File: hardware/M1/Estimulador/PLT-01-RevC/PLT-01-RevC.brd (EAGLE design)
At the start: 92.7 x 64.8 mm, 57 parts, among them T1 2N2222, T2 2N2222, T3 2N2222, T4 2N2222, T5 2N2222, T6 2N2222

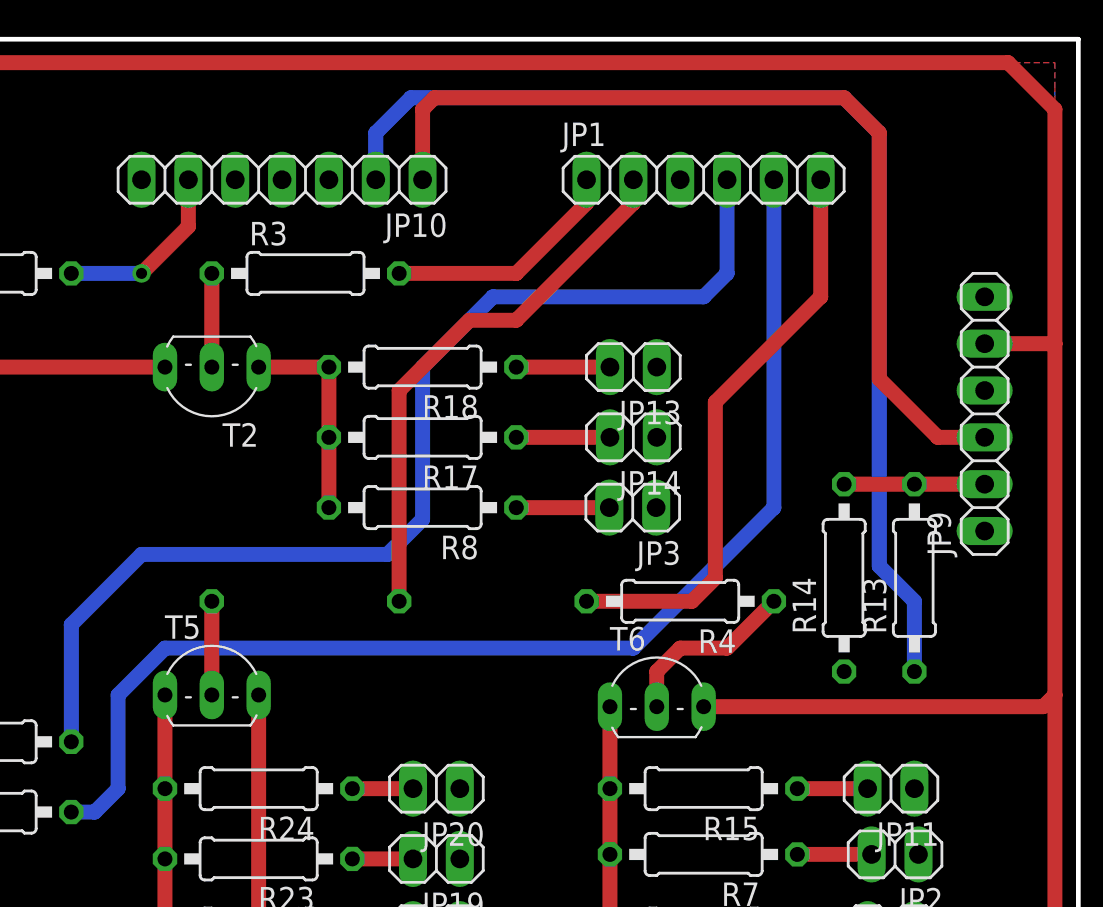
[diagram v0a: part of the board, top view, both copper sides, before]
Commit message: Se sube RevC de placa M1
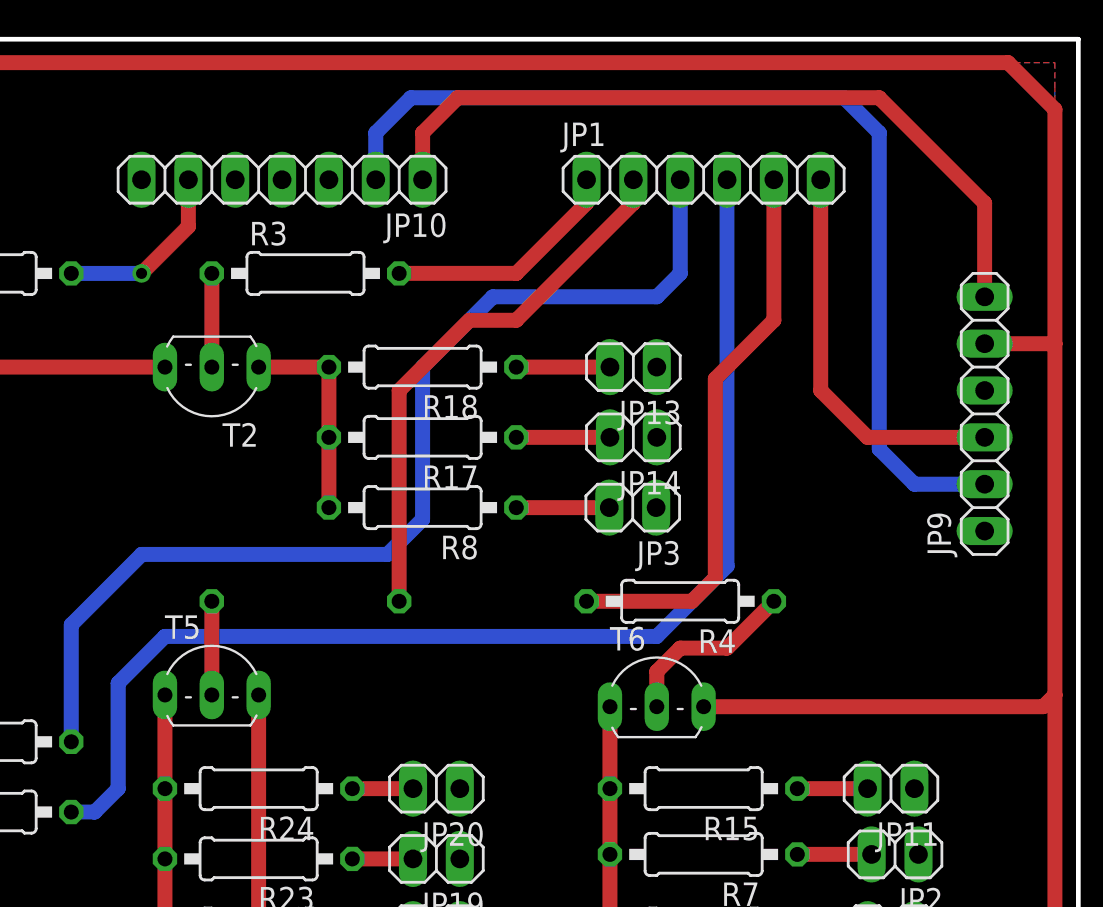
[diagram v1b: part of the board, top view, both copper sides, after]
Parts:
- removed R13, R14: (no value), resistor:0207/10
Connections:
- removed net N$26: JP9.2, R13.2, R14.2
- removed net N$27: JP10.1, JP9.3
- new net EN: JP10.1, JP9.6
- new net TX: JP1.6, JP9.3
- net GND: no longer R14.1
- net N$1: now also JP1.5; no longer JP1.6
- net N$25: now also JP9.2; no longer R13.1
- net N$4: now also JP1.3; no longer JP1.4
- net N$5: now also JP1.4; no longer JP1.5
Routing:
- net N$27: track 50.0 -> 0.00 mm
- net EN: track 0.00 -> 41.3 mm
- net TX: track 0.00 -> 21.4 mm
- net N$26: track 7.62 -> 0.00 mm
- net N$25: track 61.4 -> 55.1 mm
- net N$4: track 59.7 -> 57.2 mm
- net N$1: track 31.5 -> 30.4 mm
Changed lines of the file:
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@@
 <element name="JP9" library="pinhead" package="1X06" value="" x="87.63" y="44.45" rot="R90"/>
 <element name="JP10" library="pinhead" package="1X07" value="" x="49.53" y="57.15" rot="R180"/>
-<element name="R13" library="resistor" package="0207/10" value="" x="83.82" y="35.56" rot="R90"/>
-<element name="R14" library="resistor" package="0207/10" value="" x="80.01" y="35.56" rot="R90"/>
 <element name="JP11" library="pinhead" package="1X02" value="" x="82.55" y="24.13" rot="R180"/>
 <element name="R15" library="resistor" package="0207/10" value="" x="72.39" y="24.13" rot="R180"/>
@@
 <signal name="N$1">
 <contactref element="R4" pad="2"/>
-<contactref element="JP1" pad="6"/>
 <wire x1="66.04" y1="34.29" x2="71.755" y2="34.29" width="0.8128" layer="1"/>
 <wire x1="71.755" y1="34.29" x2="73.025" y2="35.56" width="0.8128" layer="1"/>
-<wire x1="73.025" y1="35.56" x2="73.025" y2="45.085" width="0.8128" layer="1"/>
-<wire x1="73.025" y1="45.085" x2="78.74" y2="50.8" width="0.8128" layer="1"/>
-<wire x1="78.74" y1="50.8" x2="78.74" y2="57.15" width="0.8128" layer="1"/>
+<wire x1="73.025" y1="35.56" x2="73.025" y2="46.355" width="0.8128" layer="1"/>
+<contactref element="JP1" pad="5"/>
+<wire x1="73.025" y1="46.355" x2="76.2" y2="49.53" width="0.8128" layer="1"/>
+<wire x1="76.2" y1="49.53" x2="76.2" y2="57.15" width="0.8128" layer="1"/>
 </signal>
 <signal name="N$2">
@@
 </signal>
 <signal name="N$4">
-<contactref element="JP1" pad="4"/>
 <contactref element="R1" pad="2"/>
-<wire x1="73.66" y1="57.15" x2="73.66" y2="52.07" width="0.8128" layer="16"/>
-<wire x1="73.66" y1="52.07" x2="72.39" y2="50.8" width="0.8128" layer="16"/>
-<wire x1="72.39" y1="50.8" x2="60.96" y2="50.8" width="0.8128" layer="16"/>
 <wire x1="60.96" y1="50.8" x2="57.15" y2="46.99" width="0.8128" layer="16"/>
 <wire x1="57.15" y1="46.99" x2="57.15" y2="38.735" width="0.8128" layer="16"/>
@@
 <wire x1="41.91" y1="36.83" x2="38.1" y2="33.02" width="0.8128" layer="16"/>
 <wire x1="38.1" y1="33.02" x2="38.1" y2="26.67" width="0.8128" layer="16"/>
+<contactref element="JP1" pad="3"/>
+<wire x1="71.12" y1="57.15" x2="71.12" y2="52.07" width="0.8128" layer="16"/>
+<wire x1="71.12" y1="52.07" x2="69.85" y2="50.8" width="0.8128" layer="16"/>
+<wire x1="69.85" y1="50.8" x2="60.96" y2="50.8" width="0.8128" layer="16"/>
 </signal>
 <signal name="N$5">
-<contactref element="JP1" pad="5"/>
 <contactref element="R5" pad="2"/>
-<wire x1="76.2" y1="57.15" x2="76.2" y2="39.37" width="0.8128" layer="16"/>
-<wire x1="76.2" y1="39.37" x2="68.58" y2="31.75" width="0.8128" layer="16"/>
-<wire x1="68.58" y1="31.75" x2="43.18" y2="31.75" width="0.8128" layer="16"/>
-<wire x1="43.18" y1="31.75" x2="40.64" y2="29.21" width="0.8128" layer="16"/>
-<wire x1="40.64" y1="29.21" x2="40.64" y2="24.13" width="0.8128" layer="16"/>
+<wire x1="69.85" y1="32.385" x2="43.18" y2="32.385" width="0.8128" layer="16"/>
+<wire x1="43.18" y1="32.385" x2="40.64" y2="29.845" width="0.8128" layer="16"/>
+<wire x1="40.64" y1="29.845" x2="40.64" y2="24.13" width="0.8128" layer="16"/>
 <wire x1="40.64" y1="24.13" x2="39.37" y2="22.86" width="0.8128" layer="16"/>
 <wire x1="39.37" y1="22.86" x2="38.1" y2="22.86" width="0.8128" layer="16"/>
+<contactref element="JP1" pad="4"/>
+<wire x1="69.85" y1="32.385" x2="73.66" y2="36.195" width="0.8128" layer="16"/>
+<wire x1="73.66" y1="36.195" x2="73.66" y2="57.15" width="0.8128" layer="16"/>
 </signal>
 <signal name="N$7">
@@
 <signal name="N$25">
 <contactref element="JP10" pad="2"/>
-<contactref element="R13" pad="1"/>
-<wire x1="83.82" y1="30.48" x2="83.82" y2="34.29" width="0.8128" layer="16"/>
-<wire x1="83.82" y1="34.29" x2="81.915" y2="36.195" width="0.8128" layer="16"/>
-<wire x1="81.915" y1="36.195" x2="81.915" y2="59.69" width="0.8128" layer="16"/>
 <wire x1="81.915" y1="59.69" x2="80.01" y2="61.595" width="0.8128" layer="16"/>
 <wire x1="80.01" y1="61.595" x2="56.515" y2="61.595" width="0.8128" layer="16"/>
 <wire x1="56.515" y1="61.595" x2="54.61" y2="59.69" width="0.8128" layer="16"/>
 <wire x1="54.61" y1="59.69" x2="54.61" y2="57.15" width="0.8128" layer="16"/>
-</signal>
-<signal name="N$26">
-<contactref element="R13" pad="2"/>
 <contactref element="JP9" pad="2"/>
-<contactref element="R14" pad="2"/>
-<wire x1="80.01" y1="40.64" x2="83.82" y2="40.64" width="0.8128" layer="1"/>
-<wire x1="83.82" y1="40.64" x2="87.63" y2="40.64" width="0.8128" layer="1"/>
-</signal>
-<signal name="N$27">
-<contactref element="JP10" pad="1"/>
-<contactref element="JP9" pad="3"/>
-<wire x1="87.63" y1="43.18" x2="85.09" y2="43.18" width="0.8128" layer="1"/>
-<wire x1="85.09" y1="43.18" x2="81.915" y2="46.355" width="0.8128" layer="1"/>
-<wire x1="81.915" y1="46.355" x2="81.915" y2="59.69" width="0.8128" layer="1"/>
-<wire x1="81.915" y1="59.69" x2="80.01" y2="61.595" width="0.8128" layer="1"/>
-<wire x1="80.01" y1="61.595" x2="57.785" y2="61.595" width="0.8128" layer="1"/>
-<wire x1="57.785" y1="61.595" x2="57.15" y2="60.96" width="0.8128" layer="1"/>
-<wire x1="57.15" y1="60.96" x2="57.15" y2="57.15" width="0.8128" layer="1"/>
+<wire x1="81.915" y1="59.69" x2="81.915" y2="42.545" width="0.8128" layer="16"/>
+<wire x1="81.915" y1="42.545" x2="83.82" y2="40.64" width="0.8128" layer="16"/>
+<wire x1="83.82" y1="40.64" x2="87.63" y2="40.64" width="0.8128" layer="16"/>
 </signal>
 <signal name="GND">
-<contactref element="R14" pad="1"/>
 <contactref element="JP9" pad="4"/>
 <contactref element="JP8" pad="2"/>
@@
 <wire x1="55.88" y1="45.72" x2="55.88" y2="34.29" width="0.8128" layer="1"/>
 </signal>
+<signal name="TX">
+<contactref element="JP9" pad="3"/>
+<contactref element="JP1" pad="6"/>
+<wire x1="87.63" y1="43.18" x2="81.28" y2="43.18" width="0.8128" layer="1"/>
+<wire x1="81.28" y1="43.18" x2="78.74" y2="45.72" width="0.8128" layer="1"/>
+<wire x1="78.74" y1="45.72" x2="78.74" y2="57.15" width="0.8128" layer="1"/>
+</signal>
+<signal name="EN">
+<contactref element="JP9" pad="6"/>
+<contactref element="JP10" pad="1"/>
+<wire x1="57.15" y1="57.15" x2="57.15" y2="59.69" width="0.8128" layer="1"/>
+<wire x1="57.15" y1="59.69" x2="59.055" y2="61.595" width="0.8128" layer="1"/>
+<wire x1="59.055" y1="61.595" x2="81.915" y2="61.595" width="0.8128" layer="1"/>
+<wire x1="81.915" y1="61.595" x2="87.63" y2="55.88" width="0.8128" layer="1"/>
+<wire x1="87.63" y1="55.88" x2="87.63" y2="50.8" width="0.8128" layer="1"/>
+</signal>
 </signals>

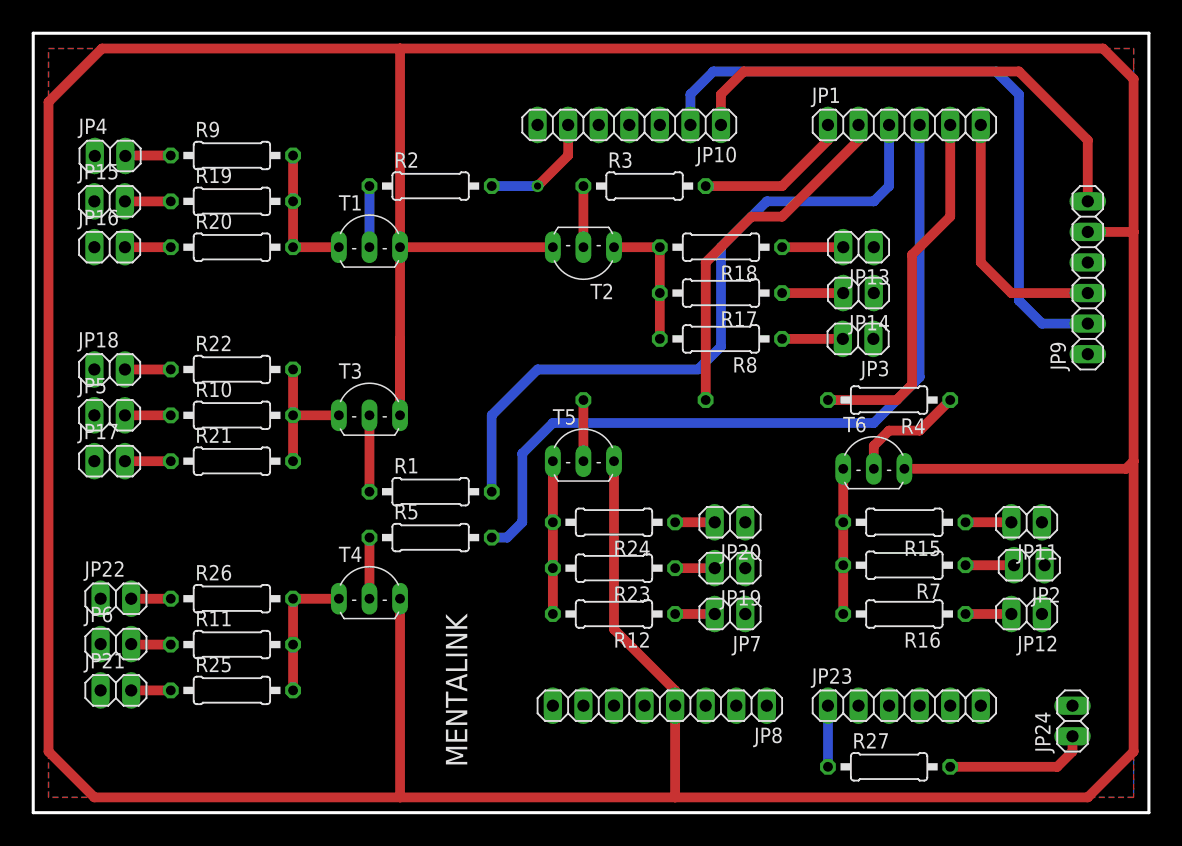
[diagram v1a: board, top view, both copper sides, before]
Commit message: Se corrige plaga RevC
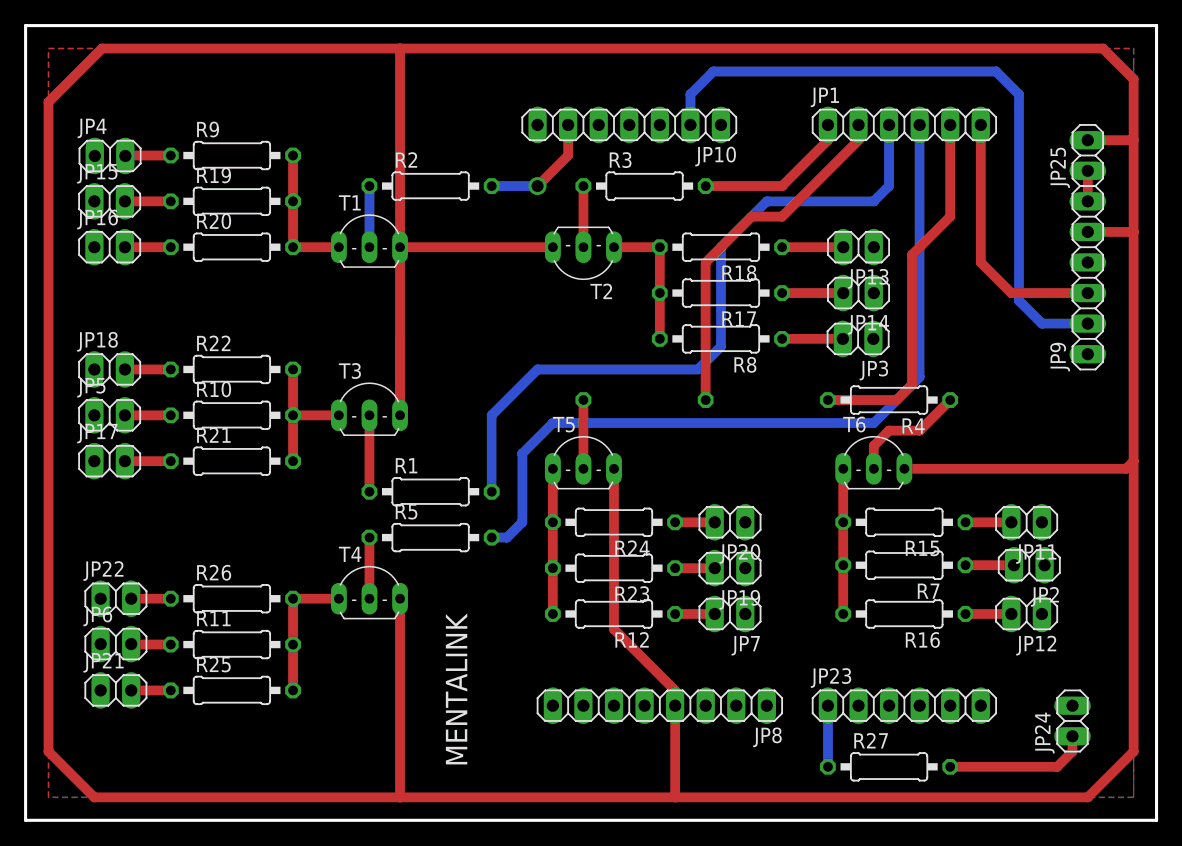
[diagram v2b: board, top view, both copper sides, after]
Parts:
- added JP25: (no value), pinhead:1X02
- moved T5 0.64 mm to (45.7, 29.8)
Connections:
- removed net EN: JP10.1, JP9.6
- new net N$6: JP25.1, JP9.6
- net 5V: now also JP25.2
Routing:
- net EN: track 41.3 -> 0.00 mm
- net 5V: track 415.5 -> 418.6 mm
- net N$6: track 0.00 -> 2.54 mm
- net N$7: track 5.08 -> 5.71 mm
- net N$23: track 12.7 -> 12.1 mm
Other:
- board size 92.7 x 64.8 mm -> 94 x 66 mm
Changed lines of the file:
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@@
 <text x="34.29" y="16.51" size="1.778" layer="25" rot="R270">MENTALINK</text>
 <text x="39.37" y="2.54" size="2.1844" layer="26" rot="R90">PLT-01-RevB</text>
-<wire x1="0" y1="64.77" x2="92.71" y2="64.77" width="0.254" layer="20"/>
-<wire x1="92.71" y1="64.77" x2="92.71" y2="0" width="0.254" layer="20"/>
-<wire x1="92.71" y1="0" x2="0" y2="0" width="0.254" layer="20"/>
-<wire x1="0" y1="0" x2="0" y2="64.77" width="0.254" layer="20"/>
+<wire x1="-0.635" y1="65.405" x2="93.345" y2="65.405" width="0.254" layer="20"/>
+<wire x1="93.345" y1="65.405" x2="93.345" y2="-0.635" width="0.254" layer="20"/>
+<wire x1="93.345" y1="-0.635" x2="-0.635" y2="-0.635" width="0.254" layer="20"/>
+<wire x1="-0.635" y1="-0.635" x2="-0.635" y2="65.405" width="0.254" layer="20"/>
 </plain>
 <attributes>
@@
 </class>
 </classes>
-<designrules name="default">
+<designrules name="default *">
 <description language="de">&lt;b&gt;EAGLE Design Rules&lt;/b&gt;
 &lt;p&gt;
@@
 <param name="mtCopper" value="0.035mm 0.035mm 0.035mm 0.035mm 0.035mm 0.035mm 0.035mm 0.035mm 0.035mm 0.035mm 0.035mm 0.035mm 0.035mm 0.035mm 0.035mm 0.035mm"/>
 <param name="mtIsolate" value="1.5mm 0.15mm 0.2mm 0.15mm 0.2mm 0.15mm 0.2mm 0.15mm 0.2mm 0.15mm 0.2mm 0.15mm 0.2mm 0.15mm 0.2mm"/>
-<param name="mdWireWire" value="8mil"/>
-<param name="mdWirePad" value="8mil"/>
-<param name="mdWireVia" value="8mil"/>
+<param name="mdWireWire" value="30mil"/>
+<param name="mdWirePad" value="30mil"/>
+<param name="mdWireVia" value="30mil"/>
 <param name="mdPadPad" value="8mil"/>
 <param name="mdPadVia" value="8mil"/>
@@
 <element name="T3" library="adafruit" package="TO92-EBC-OVAL" value="2N2222" x="27.94" y="34.29"/>
 <element name="T4" library="adafruit" package="TO92-EBC-OVAL" value="2N2222" x="27.94" y="19.05"/>
-<element name="T5" library="adafruit" package="TO92-EBC-OVAL" value="2N2222" x="45.72" y="30.48"/>
+<element name="T5" library="adafruit" package="TO92-EBC-OVAL" value="2N2222" x="45.72" y="29.845"/>
 <element name="T6" library="adafruit" package="TO92-EBC-OVAL" value="2N2222" x="69.85" y="29.845"/>
 <element name="JP8" library="pinhead" package="1X08" value="" x="52.07" y="8.89" rot="R180"/>
@@
 <element name="R27" library="resistor" package="0207/10" value="" x="71.12" y="3.81"/>
 <element name="JP24" library="pinhead" package="1X02" value="" x="86.36" y="7.62" rot="R90"/>
+<element name="JP25" library="pinhead" package="1X02" value="" x="87.63" y="54.61" rot="R90"/>
 </elements>
 <signals>
@@
 <wire x1="41.91" y1="52.07" x2="44.45" y2="54.61" width="0.8128" layer="1"/>
 <wire x1="44.45" y1="54.61" x2="44.45" y2="57.15" width="0.8128" layer="1"/>
-<via x="41.91" y="52.07" extent="1-16" drill="0.6" shape="square"/>
+<via x="41.91" y="52.07" extent="1-16" drill="1" shape="square"/>
 </signal>
 <signal name="N$4">
@@
 <contactref element="R6" pad="1"/>
 <contactref element="T5" pad="B"/>
-<wire x1="45.72" y1="34.29" x2="45.72" y2="29.21" width="0.8128" layer="1"/>
+<wire x1="45.72" y1="34.29" x2="45.72" y2="28.575" width="0.8128" layer="1"/>
 </signal>
 <signal name="N$8">
@@
 <contactref element="R23" pad="2"/>
 <contactref element="T5" pad="E"/>
-<wire x1="43.18" y1="29.21" x2="43.18" y2="24.13" width="0.8128" layer="1"/>
+<wire x1="43.18" y1="28.575" x2="43.18" y2="24.13" width="0.8128" layer="1"/>
 <wire x1="43.18" y1="24.13" x2="43.18" y2="20.32" width="0.8128" layer="1"/>
 <wire x1="43.18" y1="20.32" x2="43.18" y2="16.51" width="0.8128" layer="1"/>
@@
 <wire x1="53.34" y1="8.89" x2="53.34" y2="10.16" width="0.8128" layer="1"/>
 <wire x1="53.34" y1="10.16" x2="48.26" y2="15.24" width="0.8128" layer="1"/>
-<wire x1="48.26" y1="15.24" x2="48.26" y2="29.21" width="0.8128" layer="1"/>
+<wire x1="48.26" y1="15.24" x2="48.26" y2="28.575" width="0.8128" layer="1"/>
 <wire x1="30.48" y1="33.02" x2="30.48" y2="39.37" width="0.8128" layer="1"/>
 <wire x1="30.48" y1="33.02" x2="30.48" y2="46.99" width="0.8128" layer="1"/>
@@
 <wire x1="91.44" y1="5.08" x2="91.44" y2="29.21" width="0.8128" layer="1"/>
 <wire x1="91.44" y1="29.21" x2="91.44" y2="48.26" width="0.8128" layer="1"/>
-<wire x1="91.44" y1="48.26" x2="91.44" y2="60.96" width="0.8128" layer="1"/>
+<wire x1="91.44" y1="48.26" x2="91.44" y2="55.88" width="0.8128" layer="1"/>
+<wire x1="91.44" y1="55.88" x2="91.44" y2="60.96" width="0.8128" layer="1"/>
 <wire x1="91.44" y1="60.96" x2="88.9" y2="63.5" width="0.8128" layer="1"/>
 <wire x1="88.9" y1="63.5" x2="30.48" y2="63.5" width="0.8128" layer="1"/>
@@
 <wire x1="90.805" y1="28.575" x2="91.44" y2="29.21" width="0.8128" layer="1"/>
 <wire x1="91.44" y1="48.26" x2="87.63" y2="48.26" width="0.8128" layer="1"/>
+<contactref element="JP25" pad="2"/>
+<wire x1="87.63" y1="55.88" x2="91.44" y2="55.88" width="0.8128" layer="1"/>
 </signal>
 <signal name="N$11">
@@
 <wire x1="78.74" y1="45.72" x2="78.74" y2="57.15" width="0.8128" layer="1"/>
 </signal>
-<signal name="EN">
+<signal name="N$6">
 <contactref element="JP9" pad="6"/>
-<contactref element="JP10" pad="1"/>
-<wire x1="57.15" y1="57.15" x2="57.15" y2="59.69" width="0.8128" layer="1"/>
-<wire x1="57.15" y1="59.69" x2="59.055" y2="61.595" width="0.8128" layer="1"/>
-<wire x1="59.055" y1="61.595" x2="81.915" y2="61.595" width="0.8128" layer="1"/>
-<wire x1="81.915" y1="61.595" x2="87.63" y2="55.88" width="0.8128" layer="1"/>
-<wire x1="87.63" y1="55.88" x2="87.63" y2="50.8" width="0.8128" layer="1"/>
+<contactref element="JP25" pad="1"/>
+<wire x1="87.63" y1="53.34" x2="87.63" y2="50.8" width="0.8128" layer="1"/>
 </signal>
 </signals>
